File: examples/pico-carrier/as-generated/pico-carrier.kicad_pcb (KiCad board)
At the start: 2 copper layers, 88 x 62 mm, 9 parts, among them J1 5V IN, J3 GP0-GP15, J4 GP16-GP28, PWR, U1 Pico

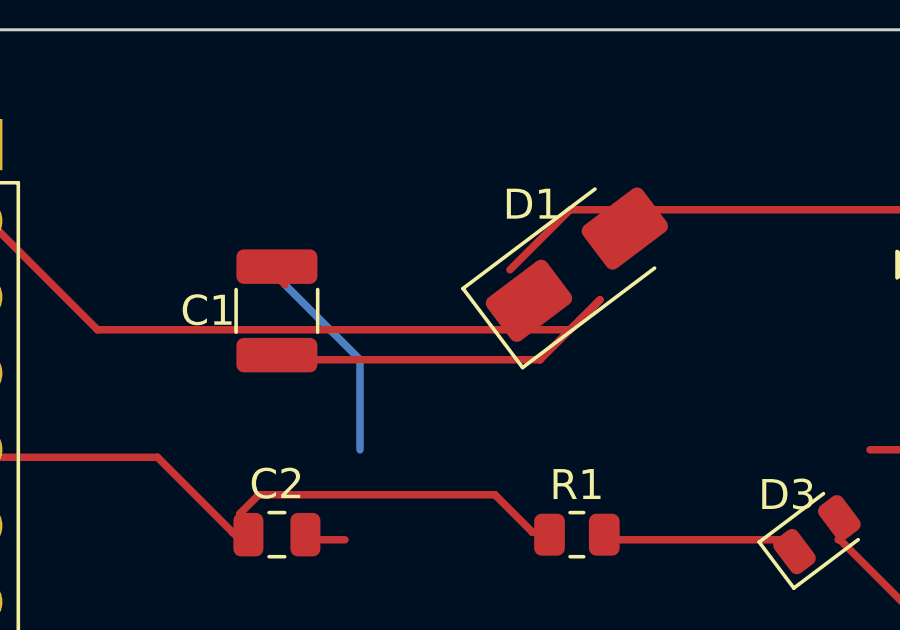
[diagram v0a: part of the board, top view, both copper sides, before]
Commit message: Stop hiding the hairpins behind the pads they are drawn on
The reviewer said the 135 degree bends and the odd-angle runs were still
there. They were. `route.acute_angle` skipped any corner within a pad's
*radius*, and a 0805's radius is 0.47 mm, which covers the five or six
ordinary corners a chamfered pad entry leaves inside it. Eleven of the
thirteen hairpins on these five boards sat in that shadow, because a pad
is exactly where a route that has to double back does it.

The exemption is the pad's connection point now, not a disc around it.
Two branches leaving one pad stay exempt - the pad's own copper fills the
wedge, so it is not an acid trap - but nought degrees never is: that is
one run drawn twice, and no pad excuses it.

Then the generator had to stop making them:

* `_untraced` drops the copper a second run lays on top of the first.
  The shorter is inside the longer and carries nothing it does not; both
  get trimmed, because dropping only the duplicate leaves the other
  hanging over the gap, which is `route.stub`. It runs before the runs
  are joined, while the pair is still two tracks sharing an end - once
  joined, the shared point is usually a pad, and the clean-up passes pin
  those precisely so they cannot take copper off them.
* `_straighten` only takes the direct line when it lands on the 45 grid.
  Between two pads at whatever coordinates their packages give them it
  usually does not: last round it made a nine millimetre run at 169.7
  degrees, which is the slip-of-the-mouse angle `route.odd_angle` is for.

Measured across the five boards: off-grid segments 1 to 0, 180 degree
reversals 6 to 0, and the motor board's `route.return_path` finding went
with the 11 mm of copper it was measuring.

Three corners survive, all on the FPGA board, all where a knee lands a
fraction past where its own two legs cross - legs of 0.07 and 0.25 mm on
two, 0.15 and 0.5 mm on the third. Refusing a knee that short is worse:
the segment then keeps the angle it had, a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
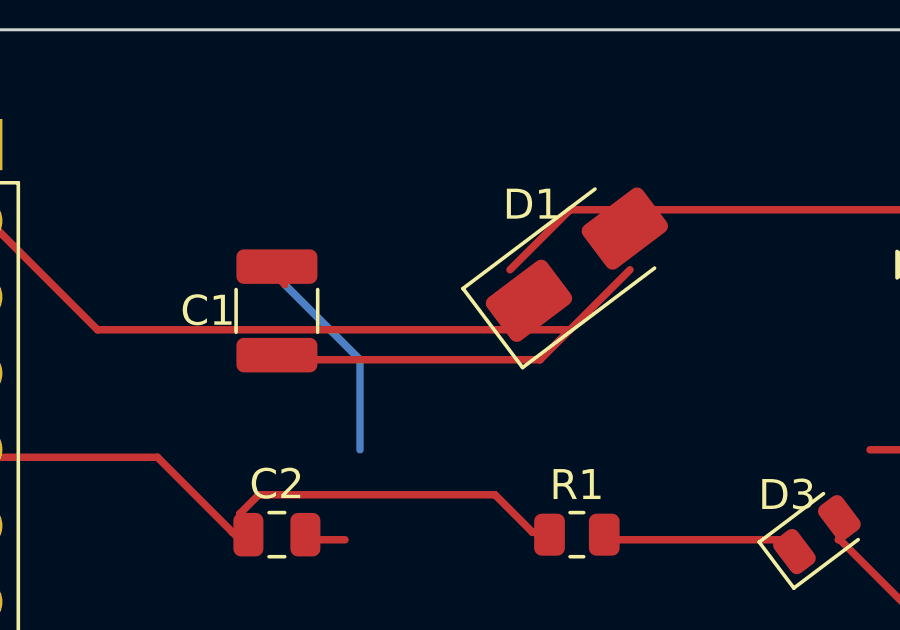
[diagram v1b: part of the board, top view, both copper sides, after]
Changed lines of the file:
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@@
 	(segment (start 142.75 66.5) (end 146.25 70.0) (width 0.25) (layer "F.Cu") (net 36))
 	(segment (start 146.25 70.0) (end 162.0 70.0) (width 0.25) (layer "F.Cu") (net 36))
-	(segment (start 162.0 70.0) (end 163.0 69.0) (width 0.25) (layer "F.Cu") (net 36))
-	(segment (start 163.0 69.0) (end 161.0 71.0) (width 0.25) (layer "F.Cu") (net 36))
-	(segment (start 161.0 71.0) (end 152.25 71.0) (width 0.25) (layer "F.Cu") (net 36))
-	(segment (start 152.25 71.0) (end 152.235 71.015) (width 0.25) (layer "F.Cu") (net 36))
-	(segment (start 152.235 71.015) (end 152.0 71.015) (width 0.25) (layer "F.Cu") (net 36))
 	(segment (start 135.69 69.08) (end 142.0 69.08) (width 0.25) (layer "F.Cu") (net 1))
 	(segment (start 135.69 71.62) (end 142.0 71.62) (width 0.25) (layer "F.Cu") (net 4))
@@
 	(segment (start 176.0 66.0) (end 162.0 66.0) (width 0.25) (layer "F.Cu") (net 3))
 	(segment (start 162.0 66.0) (end 160.0 68.0) (width 0.25) (layer "F.Cu") (net 3))
+	(segment (start 152.0 71.015) (end 152.235 71.015) (width 0.25) (layer "F.Cu") (net 36))
+	(segment (start 152.235 71.015) (end 152.25 71.0) (width 0.25) (layer "F.Cu") (net 36))
+	(segment (start 152.25 71.0) (end 161.0 71.0) (width 0.25) (layer "F.Cu") (net 36))
+	(segment (start 161.0 71.0) (end 164.0 68.0) (width 0.25) (layer "F.Cu") (net 36))
 	(segment (start 162.9125 77.0) (end 169.0625 77.0) (width 0.25) (layer "F.Cu") (net 33))
 	(segment (start 152.0 68.065) (end 152.065 68.065) (width 0.25) (layer "F.Cu") (net 1))
